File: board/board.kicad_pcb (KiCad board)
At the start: 4 copper layers, 29 x 13 mm, 8 parts, among them J1 023_LED, J2 023_LED

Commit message: Add footrpint, symbol and 3d model
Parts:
- J1, J2: value 023_LED -> osf.011
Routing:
- net (no net): vias 1 -> 0
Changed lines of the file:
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@@
       (effects (font (size 0.5 0.5) (thickness 0.05)))
     )
-    (fp_text value "023_LED" (at 5.588 2.05 180) (layer "F.Fab")
+    (fp_text value "osf.011" (at 5.588 2.05 180) (layer "F.Fab")
       (effects (font (size 0.5 0.5) (thickness 0.05)))
     )
@@
       (effects (font (size 0.5 0.5) (thickness 0.05)))
     )
-    (fp_text value "023_LED" (at 5.588 -2.5 unlocked) (layer "F.Fab")
+    (fp_text value "osf.011" (at 5.588 -2.5 unlocked) (layer "F.Fab")
       (effects (font (size 0.5 0.5) (thickness 0.05)))
     )
@@
     (property "Sheetname" "")
     (attr smd)
-    (fp_text reference "D1" (at -4.3275 -1.565) (layer "F.SilkS")
+    (fp_text reference "D1" (at 0.635 -4.445) (layer "F.SilkS")
       (effects (font (size 1 1) (thickness 0.15)))
     )
-    (fp_text value "GW_J9LHS1.4M-C1C7-2+58+MQ+30A-1-100-R33" (at 24.765 4.445) (layer "F.Fab")
+    (fp_text value "GW_J9LHS1.4M-C1C7-2+58+MQ+30A-1-100-R33" (at -3.0475 7.315) (layer "F.Fab")
       (effects (font (size 1 1) (thickness 0.15)))
     )
+    (fp_poly (pts
+        (xy -0.55 0.8)
+        (xy 1.02 0.8)
+        (xy 1.02 0.95)
+        (xy 2.6 0.95)
+        (xy 2.6 0.18)
+        (xy -0.55 0.18)
+      ) (layer "F.Paste") (width 0.01) (fill solid))
+    (fp_poly (pts
+        (xy -2.6 0.19)
+        (xy -0.95 0.19)
+        (xy -0.95 0.73)
+        (xy -1.8 0.73)
+        (xy -2.6 0.93)
+      ) (layer "F.Paste") (width 0.01) (fill solid))
+    (fp_poly (pts
+        (xy -2.6 2.15)
+        (xy 0.62 2.15)
+        (xy 0.62 1.14)
+        (xy -1.63 1.14)
+        (xy -2.6 1.45)
+      ) (layer "F.Paste") (width 0.01) (fill solid))
     (fp_poly (pts
         (xy -2.6 -2.15)
@@
         (xy -1.63 -1.14)
         (xy -2.6 -1.45)
-      ) (layer "F.Paste") (width 0.01) (fill solid))
-    (fp_poly (pts
-        (xy -2.6 0.19)
-        (xy -0.95 0.19)
-        (xy -0.95 0.73)
-        (xy -1.8 0.73)
-        (xy -2.6 0.93)
       ) (layer "F.Paste") (width 0.01) (fill solid))
     (fp_poly (pts
@@
       ) (layer "F.Paste") (width 0.01) (fill solid))
     (fp_poly (pts
-        (xy 1.02 1.35)
-        (xy 2.6 1.35)
-        (xy 2.6 2.15)
-        (xy 1.02 2.15)
-      ) (layer "F.Paste") (width 0.01) (fill solid))
-    (fp_poly (pts
-        (xy 1.02 -2.15)
-        (xy 2.6 -2.15)
-        (xy 2.6 -1.35)
-        (xy 1.02 -1.35)
-      ) (layer "F.Paste") (width 0.01) (fill solid))
-    (fp_poly (pts
         (xy -2.6 -0.19)
         (xy -0.95 -0.19)
@@
       ) (layer "F.Paste") (width 0.01) (fill solid))
     (fp_poly (pts
-        (xy -2.6 2.15)
-        (xy 0.62 2.15)
-        (xy 0.62 1.14)
-        (xy -1.63 1.14)
-        (xy -2.6 1.45)
+        (xy 1.02 -2.15)
+        (xy 2.6 -2.15)
+        (xy 2.6 -1.35)
+        (xy 1.02 -1.35)
       ) (layer "F.Paste") (width 0.01) (fill solid))
     (fp_poly (pts
-        (xy -0.55 0.8)
-        (xy 1.02 0.8)
-        (xy 1.02 0.95)
-        (xy 2.6 0.95)
-        (xy 2.6 0.18)
-        (xy -0.55 0.18)
+        (xy 1.02 1.35)
+        (xy 2.6 1.35)
+        (xy 2.6 2.15)
+        (xy 1.02 2.15)
       ) (layer "F.Paste") (width 0.01) (fill solid))
     (fp_line (start 2.6 2.52) (end -2.6 2.52) (layer "F.SilkS") (width 0.127))
     (fp_line (start -2.6 -2.52) (end 2.6 -2.52) (layer "F.SilkS") (width 0.127))
     (fp_circle (center -3.3 -1.9) (end -3.2 -1.9) (layer "F.SilkS") (width 0.2) (fill none))
-    (fp_poly (pts
-        (xy 0.97 -2.2)
-        (xy 2.65 -2.2)
-        (xy 2.65 -1.3)
-        (xy 0.97 -1.3)
-      ) (layer "F.Mask") (width 0.01) (fill solid))
-    (fp_poly (pts
-        (xy -2.65 2.2)
-        (xy 0.67 2.2)
-        (xy 0.67 1.09)
-        (xy -1.625 1.09)
-        (xy -2.65 1.42)
-      ) (layer "F.Mask") (width 0.01) (fill solid))
     (fp_poly (pts
         (xy -0.6 0.85)
@@
       ) (layer "F.Mask") (width 0.01) (fill solid))
     (fp_poly (pts
-        (xy -0.9 -0.79)
-        (xy -0.9 -0.15)
-        (xy -2.65 -0.15)
-        (xy -2.65 -1)
-        (xy -1.8 -0.79)
-      ) (layer "F.Mask") (width 0.01) (fill solid))
-    (fp_poly (pts
-        (xy -0.9 0.79)
-        (xy -0.9 0.15)
-        (xy -2.65 0.15)
-        (xy -2.65 1)
-        (xy -1.8 0.79)
-      ) (layer "F.Mask") (width 0.01) (fill solid))
-    (fp_poly (pts
-        (xy 0.97 1.3)
-        (xy 2.65 1.3)
-        (xy 2.65 2.2)
-        (xy 0.97 2.2)
+        (xy -2.65 2.2)
+        (xy 0.67 2.2)
+        (xy 0.67 1.09)
+        (xy -1.625 1.09)
+        (xy -2.65 1.42)
       ) (layer "F.Mask") (width 0.01) (fill solid))
     (fp_poly (pts
@@
         (xy -1.625 -1.09)
         (xy -2.65 -1.42)
+      ) (layer "F.Mask") (width 0.01) (fill solid))
+    (fp_poly (pts
+        (xy 0.97 -2.2)
+        (xy 2.65 -2.2)
+        (xy 2.65 -1.3)
+        (xy 0.97 -1.3)
       ) (layer "F.Mask") (width 0.01) (fill solid))
     (fp_poly (pts
@@
         (xy -0.6 -0.13)
       ) (layer "F.Mask") (width 0.01) (fill solid))
+    (fp_poly (pts
+        (xy -0.9 -0.79)
+        (xy -0.9 -0.15)
+        (xy -2.65 -0.15)
+        (xy -2.65 -1)
+        (xy -1.8 -0.79)
+      ) (layer "F.Mask") (width 0.01) (fill solid))
+    (fp_poly (pts
+        (xy -0.9 0.79)
+        (xy -0.9 0.15)
+        (xy -2.65 0.15)
+        (xy -2.65 1)
+        (xy -1.8 0.79)
+      ) (layer "F.Mask") (width 0.01) (fill solid))
+    (fp_poly (pts
+        (xy 0.97 1.3)
+        (xy 2.65 1.3)
+        (xy 2.65 2.2)
+        (xy 0.97 2.2)
+      ) (layer "F.Mask") (width 0.01) (fill solid))
     (fp_line (start 2.9 2.75) (end -2.9 2.75) (layer "F.CrtYd") (width 0.05))
     (fp_line (start -2.9 -2.75) (end 2.9 -2.75) (layer "F.CrtYd") (width 0.05))
+    (fp_line (start 2.9 -2.75) (end 2.9 2.75) (layer "F.CrtYd") (width 0.05))
     (fp_line (start -2.9 2.75) (end -2.9 -2.75) (layer "F.CrtYd") (width 0.05))
-    (fp_line (start 2.9 -2.75) (end 2.9 2.75) (layer "F.CrtYd") (width 0.05))
     (fp_line (start -2.6 2.5) (end -2.6 -2.5) (layer "F.Fab") (width 0.127))
+    (fp_line (start 2.6 2.5) (end -2.6 2.5) (layer "F.Fab") (width 0.127))
     (fp_line (start -2.6 -2.5) (end 2.6 -2.5) (layer "F.Fab") (width 0.127))
-    (fp_line (start 2.6 2.5) (end -2.6 2.5) (layer "F.Fab") (width 0.127))
     (fp_line (start 2.6 -2.5) (end 2.6 2.5) (layer "F.Fab") (width 0.127))
     (fp_circle (center -3.3 -1.9) (end -3.2 -1.9) (layer "F.Fab") (width 0.2) (fill none))
@@
     (pad "8" smd rect locked (at 1.81 -1.75) (size 1.68 0.9) (layers "F.Cu")
       (net 5 "Net-(D1-Pad8)") (pintype "passive"))
+    (model "//wsl.localhost/Arch/home/niklas/led_edgy/led_edgy.pretty/GW_J9LHS1.4M-C1C7-2_58_MQ_30A-1-100-R33.step"
+      (offset (xyz 0 0 0))
+      (scale (xyz 1 1 1))
+      (rotate (xyz -90 0 0))
+    )
   )
   (footprint "Resistor_SMD:R_0603_1608Metric_Pad0.98x0.95mm_HandSolder" (layer "F.Cu")
@@
   (gr_line (start 169 101) (end 169 100.5) (layer "Edge.Cuts") (width 0.05))
   (gr_line (start 140 92.5) (end 140 92) (layer "Edge.Cuts") (width 0.05))
-  (via (at 154.55 97.1) (size 0.5) (drill 0.2) (layers "F.Cu" "B.Cu") (free) (net 0))
-  (segment (start 149.8375 94.5) (end 149.3875 94.95) (width 0.2) (layer "F.Cu") (net 1))
-  (segment (start 151.02 94.5) (end 149.8375 94.5) (width 0.2) (layer "F.Cu") (net 1))
+  (segment (start 149.92 94.5) (end 149.71 94.71) (width 0.2) (layer "F.Cu") (net 1))
+  (segment (start 151.02 94.5) (end 149.92 94.5) (width 0.2) (layer "F.Cu") (net 1))
   (segment (start 156.1775 95.075) (end 155.25 95.075) (width 0.2) (layer "F.Cu") (net 1))
   (segment (start 155.25 95.075) (end 154.675 94.5) (width 0.2) (layer "F.Cu") (net 1))
@@
   (segment (start 154.7 97.825) (end 154.475 98.05) (width 0.2) (layer "B.Cu") (net 13))
   (segment (start 165.2 91.025) (end 166.65 92.475) (width 0.2) (layer "F.Cu") (net 14))
-  (segment (start 144.4005 90.4495) (end 142.35 92.5) (width 0.2) (layer "F.Cu") (net 14))
+  (segment (start 143.90525 90.94475) (end 142.35 92.5) (width 0.2) (layer "F.Cu") (net 14))
   (segment (start 166.65 92.475) (end 166.65 92.5) (width 0.2) (layer "F.Cu") (net 14))
-  (via (at 144.4005 90.4495) (size 0.5) (drill 0.2) (layers "F.Cu" "B.Cu") (net 14))
+  (via (at 143.90525 90.94475) (size 0.5) (drill 0.2) (layers "F.Cu" "B.Cu") (net 14))
   (via (at 165.2 91.025) (size 0.5) (drill 0.2) (layers "F.Cu" "B.Cu") (net 14))
-  (segment (start 144.4005 90.4495) (end 144.525 90.325) (width 0.2) (layer "B.Cu") (net 14))
+  (segment (start 144.525 90.325) (end 164.5 90.325) (width 0.2) (layer "B.Cu") (net 14))
   (segment (start 164.5 90.325) (end 165.2 91.025) (width 0.2) (layer "B.Cu") (net 14))
-  (segment (start 144.525 90.325) (end 164.5 90.325) (width 0.2) (layer "B.Cu") (net 14))
+  (segment (start 143.90525 90.94475) (end 144.525 90.325) (width 0.2) (layer "B.Cu") (net 14))
   (zone (net 10) (net_name "Net-(J1-Pad10)") (layers "F.Cu" "In1.Cu" "In2.Cu" "B.Cu") (hatch edge 0.508)
     (connect_pads (clearance 0.508))

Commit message: Add open hardware logo
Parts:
- moved LOGO1 25.7 mm to (148.7, 99.9)
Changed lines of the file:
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@@
   )
   (footprint "Symbol:OSHW-Symbol_6.7x6mm_SilkScreen" (layer "B.Cu")
-    (at 132.5 119.95 180)
+    (at 148.65 99.94 180)
     (descr "Open Source Hardware Symbol")
     (tags "Logo Symbol OSHW")

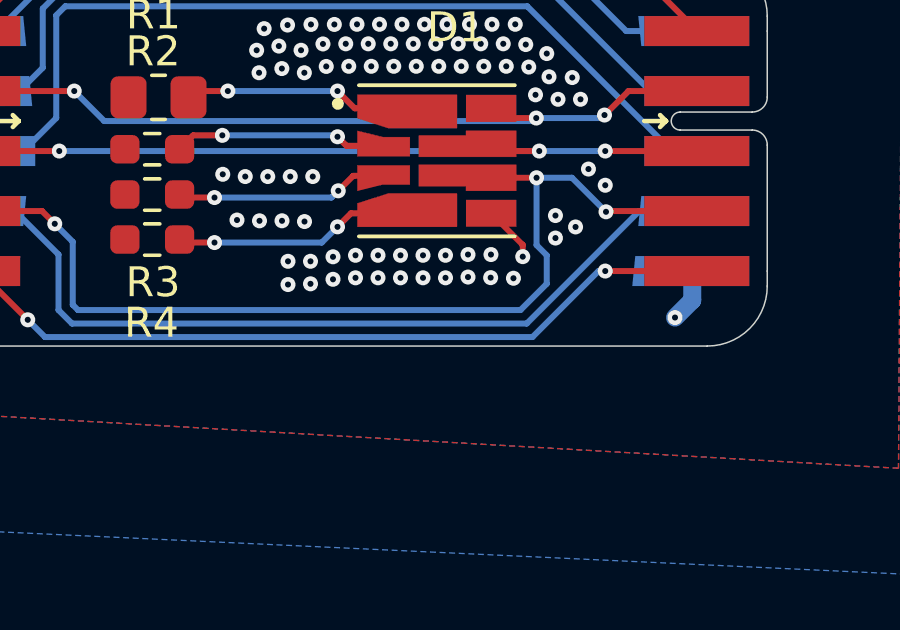
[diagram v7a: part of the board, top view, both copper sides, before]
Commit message: Add silkscreen for identification
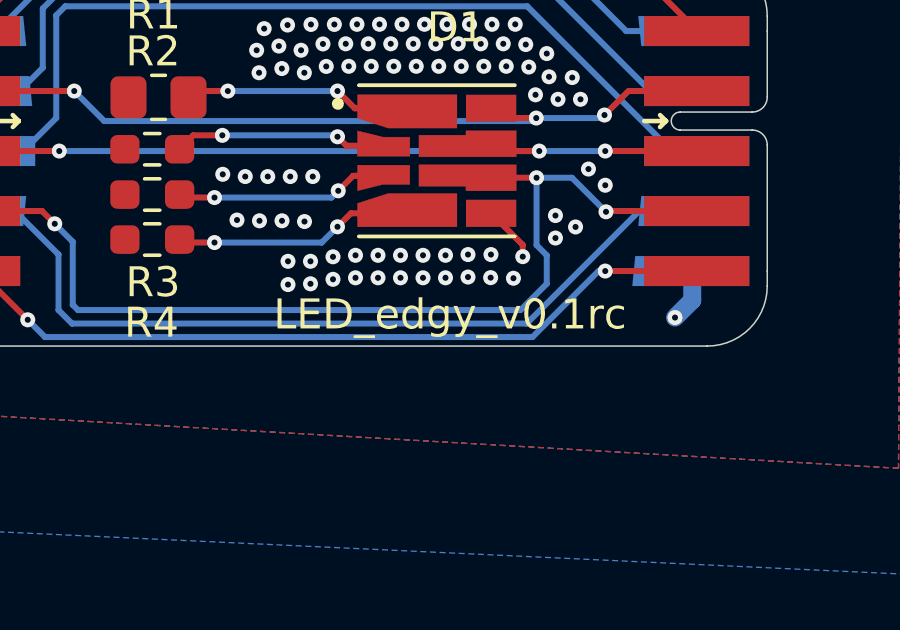
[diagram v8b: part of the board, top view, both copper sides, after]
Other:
- board text added: "LED_edgy_v0.1rc"
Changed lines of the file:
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@@
       (effects (font (size 1 1) (thickness 0.15)))
     )
-    (fp_text value "GW_J9LHS1.4M-C1C7-2+58+MQ+30A-1-100-R33" (at -3.0475 7.315) (layer "F.Fab")
+    (fp_text value "GW_J9LHS1.4M-C1C7-2+58+MQ+30A-1-100-R33" (at -0.0875 8.15) (layer "F.Fab")
       (effects (font (size 1 1) (thickness 0.15)))
     )
@@
   (gr_line (start 169 101) (end 169 100.5) (layer "Edge.Cuts") (width 0.05))
   (gr_line (start 140 92.5) (end 140 92) (layer "Edge.Cuts") (width 0.05))
+  (gr_text "LED_edgy_v0.1rc" (at 158.425 101.95) (layer "F.SilkS")
+    (effects (font (size 1 1) (thickness 0.15)))
+  )
   (segment (start 149.92 94.5) (end 149.71 94.71) (width 0.2) (layer "F.Cu") (net 1))
   (segment (start 151.02 94.5) (end 149.92 94.5) (width 0.2) (layer "F.Cu") (net 1))
